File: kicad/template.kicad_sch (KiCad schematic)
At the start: 7 parts, among them J1 Bus_PCI_Express_x1, J6 USB_C_Receptacle_USB2.0_16P, U1 MCP25625T-E/ML, U2 RP2040, U4 W25Q128JVP, X1 ABM8-272-T3, Y1 X322516MLB4SI

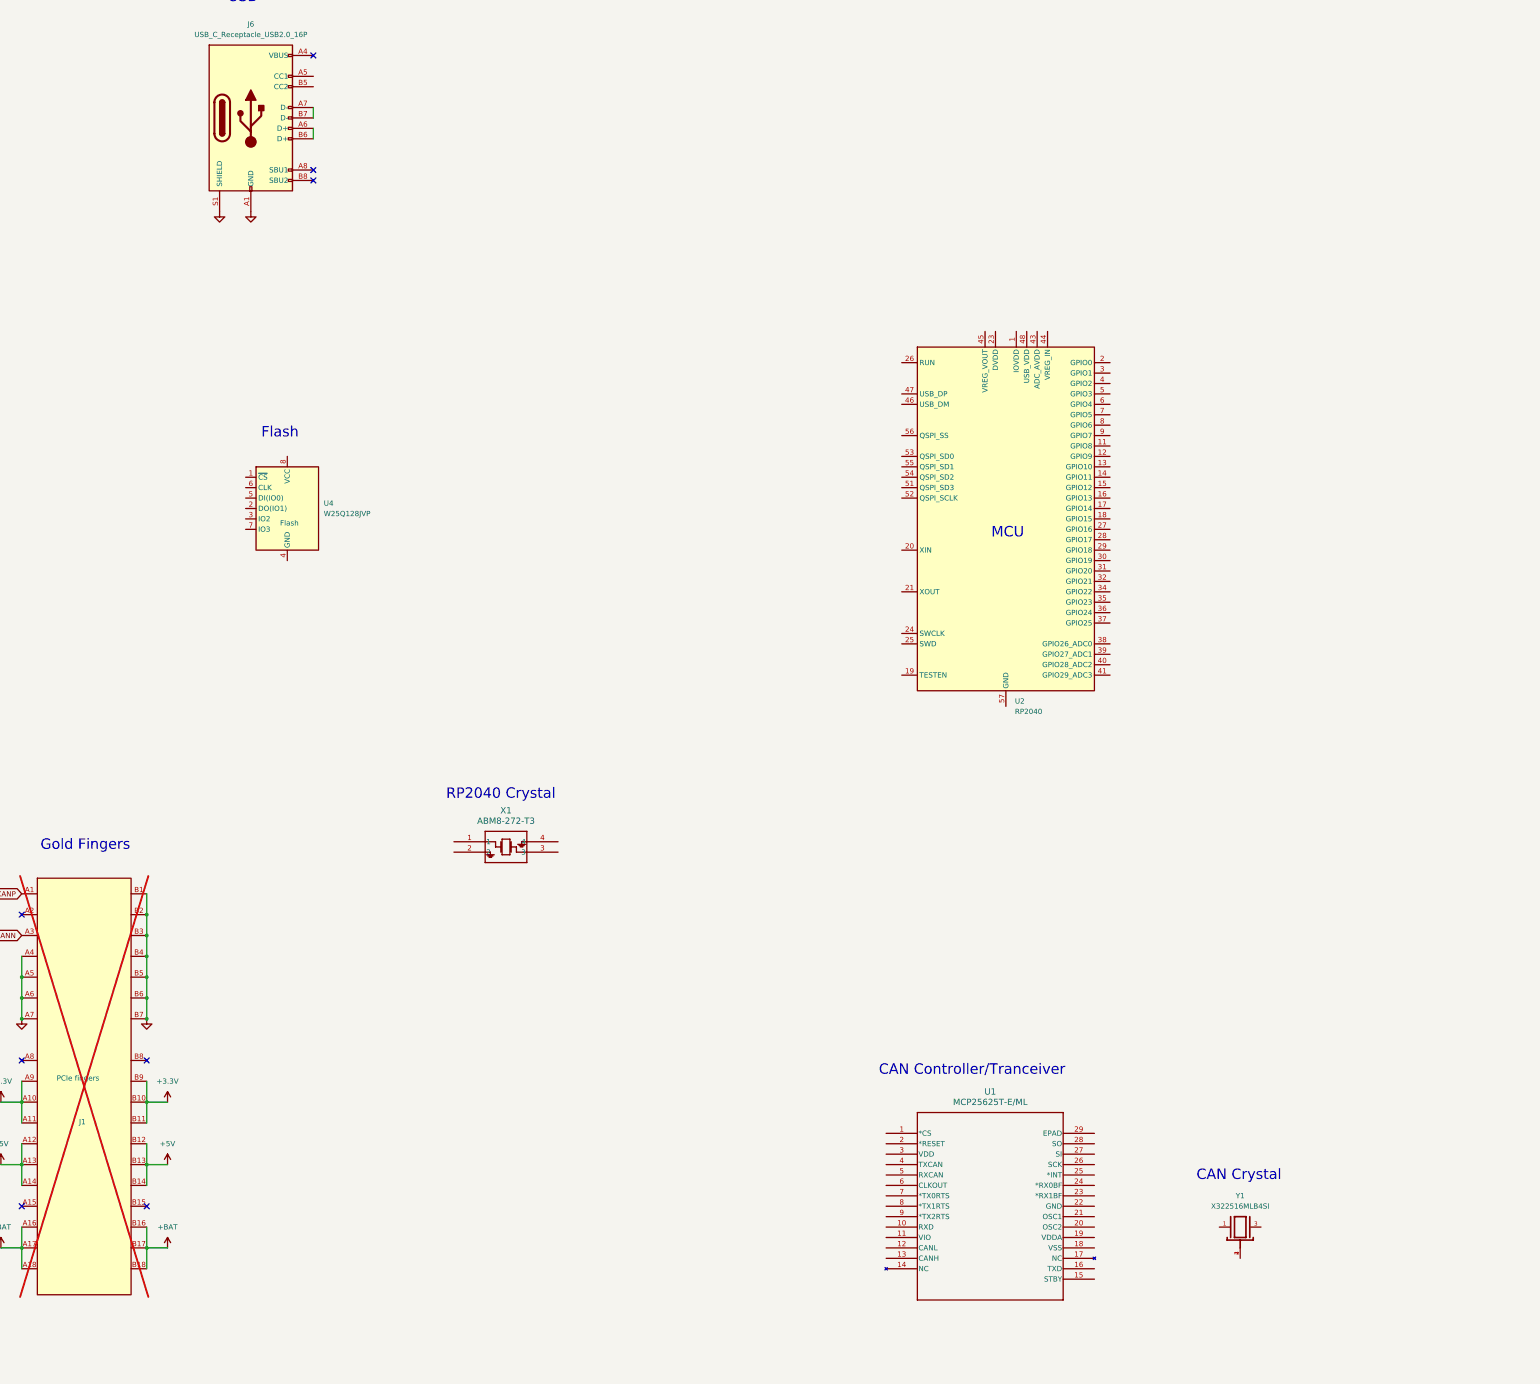
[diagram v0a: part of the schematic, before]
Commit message: Add LED array
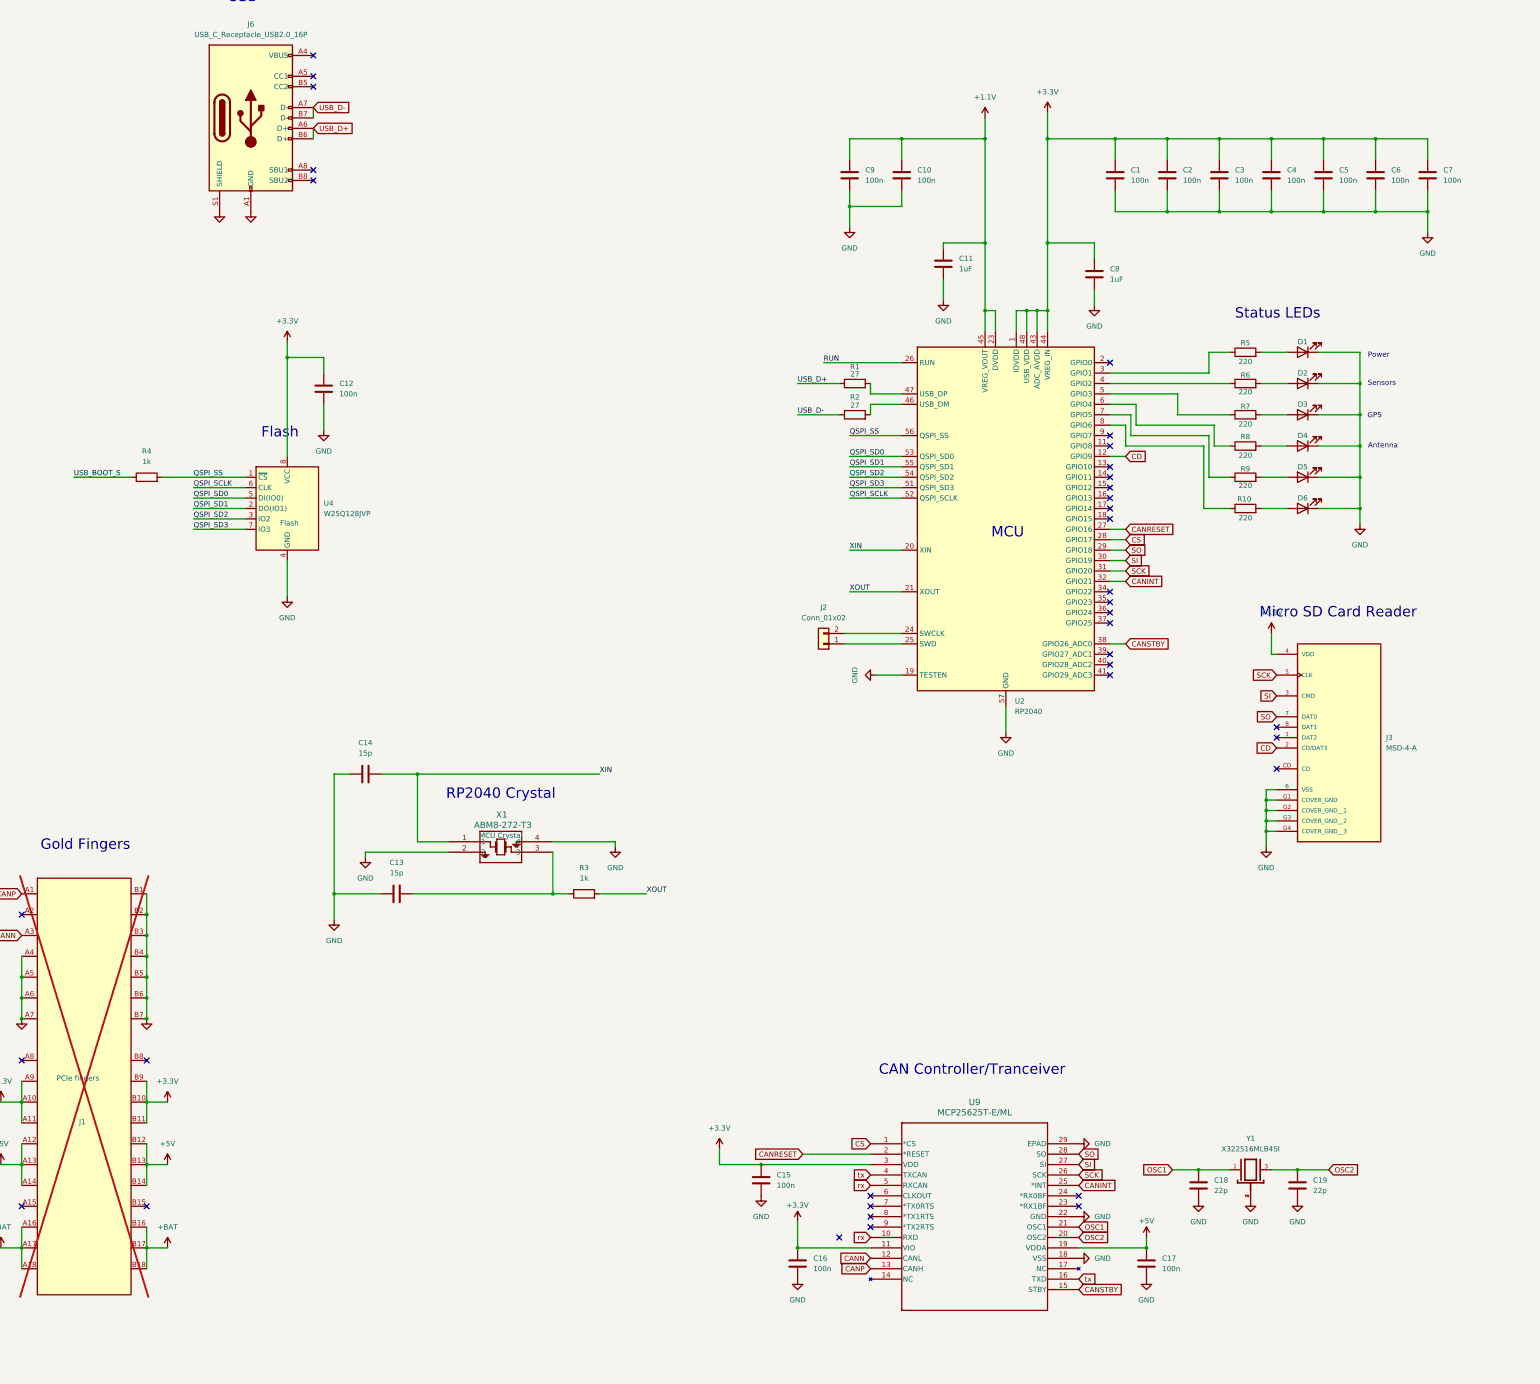
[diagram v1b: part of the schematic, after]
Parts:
- removed U1: MCP25625T-E/ML, challenge_template:QFN28_6X6MC_MCH, symbol challenge symbols:MCP25625T-E_ML
- removed X1: ABM8-272-T3, challenge_template:ABM8-272-T3_ABR, symbol challenge symbols:ABM8-272-T3
- removed Y1: X322516MLB4SI, challenge_template:OSC_X322516MLB4SI, symbol challenge symbols:X322516MLB4SI
- added C1, C10, C15, C16, C17, C2, C3, C4, C5, C6, C7, C9: 100n, Capacitor_SMD:C_0402_1005Metric, symbol Device:C
- added C11, C8: 1uF, Capacitor_SMD:C_0402_1005Metric, symbol Device:C
- added C12: 100n, Capacitor_SMD:C_0603_1608Metric, symbol Device:C
- added C13, C14: 15p, Capacitor_SMD:C_0603_1608Metric, symbol Device:C
- added C18, C19: 22p, Capacitor_SMD:C_0603_1608Metric, symbol Device:C
- added D1, D2, D3, D4, D5, D6: LED, LED_SMD:LED_0805_2012Metric, symbol Device:LED
- added J2: Conn_01x02, Connector_JST:JST_EH_B2B-EH-A_1x02_P2.50mm_Vertical, symbol Connector_Generic:Conn_01x02
- added J3: MSD-4-A, MSD_4_A:CUI_MSD-4-A, symbol MSD-4-A:MSD-4-A
- added R1, R2: 27, Resistor_SMD:R_0402_1005Metric, symbol Device:R
- added R10, R5, R6, R7, R8, R9: 220, Resistor_SMD:R_0603_1608Metric, symbol Device:R
- added R3, R4: 1k, Resistor_SMD:R_0603_1608Metric, symbol Device:R
- added U9: MCP25625T-E/ML, MCP25625T_E_ML:QFN28_6X6MC_MCH, symbol MCP25625:MCP25625T-E_ML
- added X1: ABM8-272-T3, ABM8-272-T3:ABM8-272-T3_ABR, symbol crystal:ABM8-272-T3
- added Y1: X322516MLB4SI, X322516MLB4SI:OSC_X322516MLB4SI, symbol X322516MLB4SI:X322516MLB4SI
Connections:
- net +3.3V: now also U2.1 (IOVDD), U2.10 (IOVDD), U2.22 (IOVDD), U2.33 (IOVDD), U2.42 (IOVDD), U2.43 (ADC_AVDD), U2.44 (VREG_IN), U2.48 (USB_VDD), U2.49 (IOVDD), U4.8 (VCC), C1.1, C12.1, C15.1, C16.1, C2.1, C3.1, C4.1, C5.1, C6.1, C7.1, C8.1, J3.4 (VDD), U9.11 (VIO), U9.3 (VDD)
- net +5V: now also C17.1, U9.19 (VDDA)
- net CANN: now also U9.12 (CANL)
- net CANP: now also U9.13 (CANH)
- net GND: now also U2.19 (TESTEN), U2.57 (GND), U4.4 (GND), C1.2, C10.2, C11.2, C12.2, C13.2, C14.1, C15.2, C16.2, C17.2, C18.2, C19.2, C2.2, C3.2, C4.2, C5.2, C6.2, C7.2, C8.2, C9.2, D1.1 (K), D2.1 (K), D3.1 (K), D4.1 (K), D5.1 (K), D6.1 (K), J3.6 (VSS), J3.G1 (COVER_GND), J3.G2 (COVER_GND__1), J3.G3 (COVER_GND__2), J3.G4 (COVER_GND__3), U9.18 (VSS), U9.22 (GND), U9.29 (EPAD), X1.2, X1.4, Y1.2, Y1.4
- net QSPI_SS: now reaches U4.1 (~{CS})
- net QSPI_SS: now also U2.56 (QSPI_SS), R4.2
- net QSPI_SD1: now reaches U4.2 (DO(IO1))
- net QSPI_SD1: now also U2.55 (QSPI_SD1)
- net QSPI_SD2: now reaches U4.3 (IO2)
- net QSPI_SD2: now also U2.54 (QSPI_SD2)
- net QSPI_SD0: now reaches U4.5 (DI(IO0))
- net QSPI_SD0: now also U2.53 (QSPI_SD0)
- net QSPI_SCLK: now reaches U4.6 (CLK)
- net QSPI_SCLK: now also U2.52 (QSPI_SCLK)
- net QSPI_SD3: now reaches U4.7 (IO3)
- net QSPI_SD3: now also U2.51 (QSPI_SD3)
- net CD: now reaches U2.12 (GPIO9)
- net CD: now also J3.2 (CD/DAT3)
- net XIN: now reaches U2.20 (XIN)
- net XIN: now also C14.2, X1.1
- net XOUT: now reaches U2.21 (XOUT)
- net XOUT: now also R3.2
- net +1.1V: now reaches U2.23 (DVDD), U2.50 (DVDD)
- net +1.1V: now also U2.45 (VREG_VOUT), C10.1, C11.1, C9.1
- net at U2.24 (SWCLK): now also J2.2 (Pin_2)
- net at U2.25 (SWD): now also J2.1 (Pin_1)
- net RUN: now reaches U2.26 (RUN)
- net CANRESET: now reaches U2.27 (GPIO16)
- net CANRESET: now also U9.2 (*RESET)
- net CS: now reaches U2.28 (GPIO17)
- net CS: now also U9.1 (*CS)
- net SO: now reaches U2.29 (GPIO18)
- net SO: now also J3.7 (DAT0), U9.28 (SO)
- net at U2.3 (GPIO1): now also R5.1
- net SI: now reaches U2.30 (GPIO19)
- net SI: now also J3.3 (CMD), U9.27 (SI)
- net SCK: now reaches U2.31 (GPIO20)
- net SCK: now also J3.5 (CLK), U9.26 (SCK)
- net CANINT: now reaches U2.32 (GPIO21)
- net CANINT: now also U9.25 (*INT)
- net CANSTBY: now reaches U2.38 (GPIO26_ADC0)
- net CANSTBY: now also U9.15 (STBY)
- net at U2.4 (GPIO2): now also R6.1
- net at U2.46 (USB_DM): now also R2.2
- net at U2.47 (USB_DP): now also R1.2
- net at U2.5 (GPIO3): now also R7.1
- net at U2.6 (GPIO4): now also R8.1
- net at U2.7 (GPIO5): now also R9.1
- net at U2.8 (GPIO6): now also R10.1
- net USB_D+: now reaches J6.A6 (D+), J6.B6 (D+)
- net USB_D+: now also R1.1
- net USB_D-: now reaches J6.A7 (D-), J6.B7 (D-)
- net USB_D-: now also R2.1
- new net: C13.1, R3.1, X1.3
- new net: D1.2 (A), R5.2
- new net: D4.2 (A), R8.2
- new net: D3.2 (A), R7.2
- new net: D2.2 (A), R6.2
- new net: D5.2 (A), R9.2
- new net: D6.2 (A), R10.2
- new net OSC1: C18.1, U9.21 (OSC1), Y1.1
- new net OSC2: C19.1, U9.20 (OSC2), Y1.3
- new net USB_BOOT_S: R4.1
- new net rx: U9.10 (RXD), U9.5 (RXCAN)
- new net tx: U9.16 (TXD), U9.4 (TXCAN)
- no-connect marks 8 -> 36
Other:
- note added: "Antenna"
- note added: "GPS"
- note added: "Micro SD Card Reader"
- note added: "Power"
- note added: "Sensors"
- note added: "Status LEDs"
- note removed: "CAN Crystal"
